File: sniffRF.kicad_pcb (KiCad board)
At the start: 4 copper layers, 113.8 x 23.3 mm, 74 parts, among them J201 USBC, J301 SWD, J401 Ant, J501 FFC_Hirose_FH12-30S-0.5SH_55_, Q501 PMOS, Q502 NMOS, SW301 Reset, U201 BQ24074RGTRG4, U202 MAX17048G+T10, U203 TPS62840DLCR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

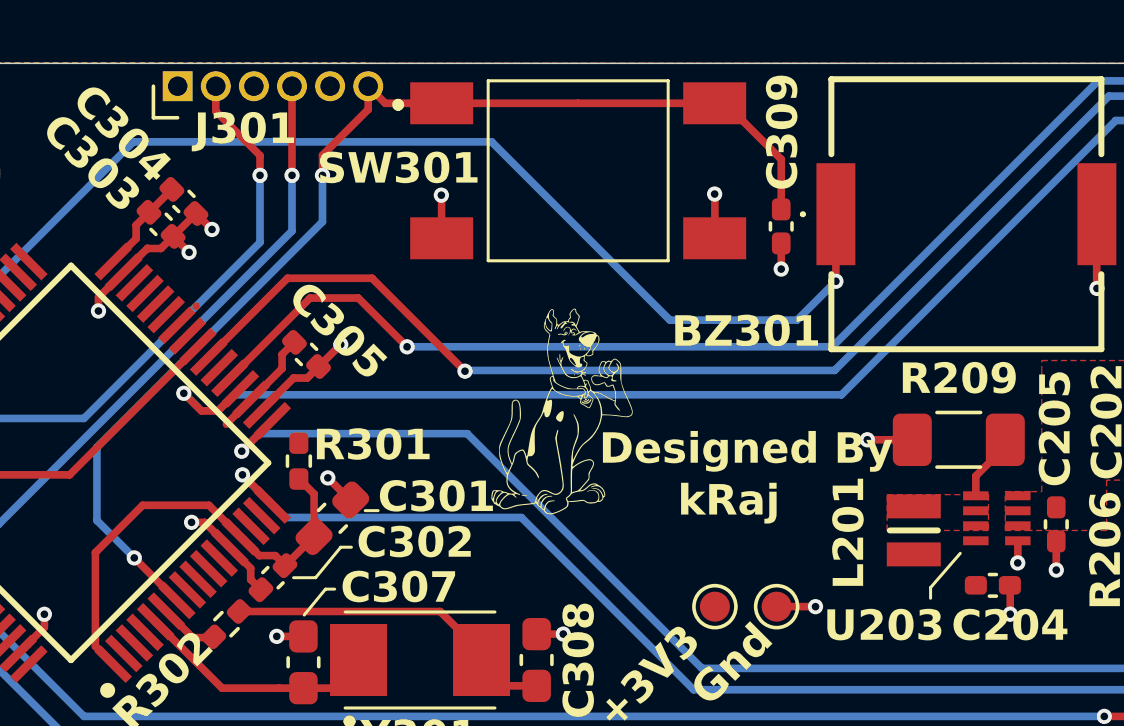
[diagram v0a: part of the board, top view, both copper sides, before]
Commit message: Updated readme and file structure, bug fixes and prep for manuf
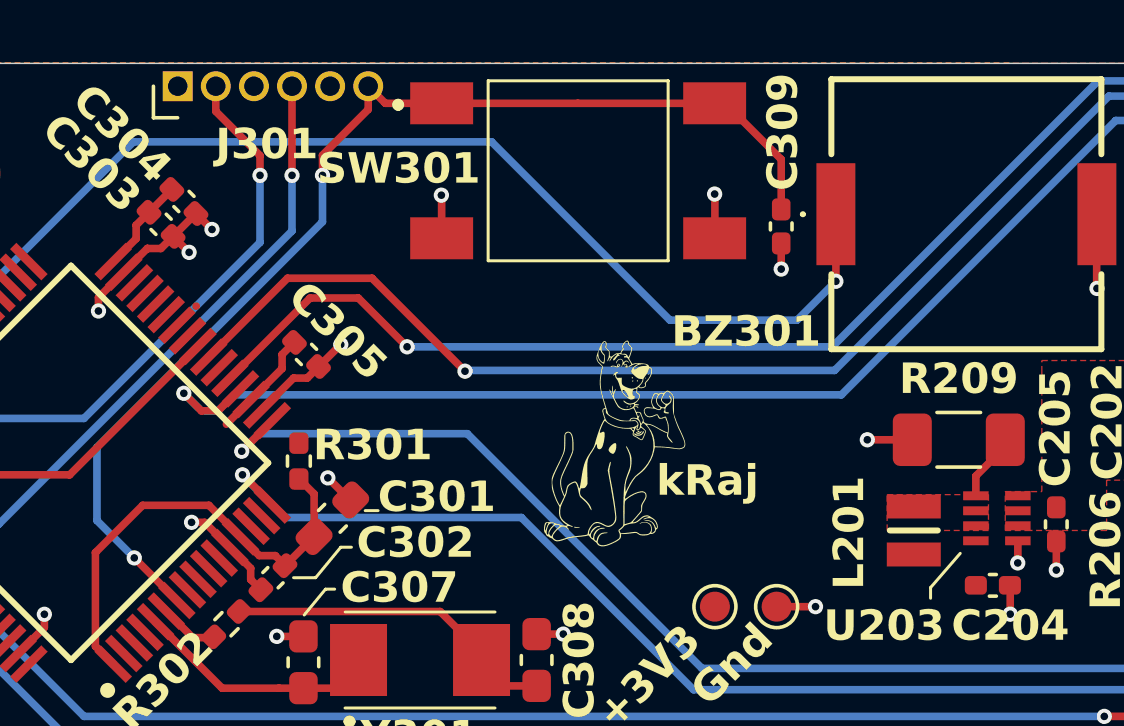
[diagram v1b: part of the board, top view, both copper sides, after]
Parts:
- moved G*** 2.05 mm to (94.7, 39.6)
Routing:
- net GNDREF: track 116.1 -> 118.8 mm
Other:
- board text removed: "Designed By"
